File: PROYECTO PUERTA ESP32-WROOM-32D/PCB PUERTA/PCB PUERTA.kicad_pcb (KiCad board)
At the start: 2 copper layers, 91.3 x 69.2 mm, 35 parts, among them J1 LIMIT SWITCHES, J2 LLAVE, J3 Screw_Terminal_01x03, J4 Screw_Terminal_01x02, J5 ALIMENTACION, J6 MOTOR, J7 LAMP, K1 FINDER-36.11, K2 FINDER-36.11, Q1 PZT2222A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

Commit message: 20.03.2025
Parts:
- removed Q1, Q2, Q3, Q4: PZT2222A, Package_TO_SOT_SMD:SOT-223-3_TabPin2
- added C2: 100nF, Capacitor_SMD:C_0402_1005Metric, B.Cu at (110.0, 84.3)
- added C3: 100nF, Capacitor_SMD:C_0402_1005Metric, B.Cu at (110.0, 91.3)
- added C4: 100nF, Capacitor_SMD:C_0402_1005Metric, B.Cu at (110.0, 80.4)
- added C5: 100nF, Capacitor_SMD:C_0402_1005Metric, B.Cu at (110.0, 87.8)
- added C6: 100nF, Capacitor_SMD:C_0402_1005Metric, B.Cu at (109.7, 72.7)
- added C7: 22uF, Capacitor_SMD:CP_Elec_5x5.4, F.Cu at (144.2, 80.5)
- added D10: MA, LED_SMD:LED_0402_1005Metric, F.Cu at (136.2, 91.6)
- added D11: MC, LED_SMD:LED_0402_1005Metric, F.Cu at (137.7, 122.2)
- added D12: MA, LED_SMD:LED_0402_1005Metric, F.Cu at (123.3, 118.8)
- added D13: MA, LED_SMD:LED_0402_1005Metric, F.Cu at (144.4, 133.6)
- added D3: ESD9B3.3ST5G, Diode_SMD:D_SOD-923, B.Cu at (109.8, 92.8)
- added D4: ESD9B3.3ST5G, Diode_SMD:D_SOD-923, B.Cu at (109.8, 81.9)
- added D5: ESD9B3.3ST5G, Diode_SMD:D_SOD-923, B.Cu at (109.8, 89.3)
- added D6: ESD9B3.3ST5G, Diode_SMD:D_SOD-923, B.Cu at (109.7, 74.1)
- added D7: 3V3, LED_SMD:LED_0402_1005Metric, F.Cu at (120.3, 125.9)
- added D8: 5V, LED_SMD:LED_0402_1005Metric, F.Cu at (123.5, 125.9)
- added D9: 12V, LED_SMD:LED_0402_1005Metric, F.Cu at (127.3, 125.9)
- added R17: 0.1, Resistor_SMD:R_2512_6332Metric, F.Cu at (135.2, 95.8)
- added R18: 220, Resistor_SMD:R_0402_1005Metric, F.Cu at (135.8, 122.2)
- added R19: 220, Resistor_SMD:R_0402_1005Metric, F.Cu at (121.4, 118.8)
- added R20: 220, Resistor_SMD:R_0402_1005Metric, F.Cu at (142.5, 133.6)
- added U2: MMUN2233LT1G, LIBRERIA PERSONAL:SOT-23-3_1P4X3P040_ONS-L, F.Cu at (135.3, 87.9)
- added U3: LM358, LIBRERIA PERSONAL:lm358, F.Cu at (135.3, 103.7)
- added U4: MMUN2233LT1G, LIBRERIA PERSONAL:SOT-23-3_1P4X3P040_ONS-L, F.Cu at (122.4, 115.4)
- added U5: MMUN2233LT1G, LIBRERIA PERSONAL:SOT-23-3_1P4X3P040_ONS-L, F.Cu at (143.5, 129.6)
- added U6: MMUN2233LT1G, LIBRERIA PERSONAL:SOT-23-3_1P4X3P040_ONS-L, F.Cu at (136.7, 118.6)
- BZ1: footprint Buzzer_Beeper:Buzzer_CUI_CPT-9019S-SMT -> Buzzer_Beeper:Buzzer_TDK_PS1240P02BT_D12.2mm_H6.5mm
- C1: value 22u -> 100nF; moved to B.Cu
- D1: value MA -> ESD9B3.3ST5G; footprint LED_SMD:LED_0402_1005Metric -> Diode_SMD:D_SOD-923; moved to B.Cu
- D2: value MC -> ESD9B3.3ST5G; footprint LED_SMD:LED_0402_1005Metric -> Diode_SMD:D_SOD-923; moved to B.Cu
- J5: value ALIMENTACION -> Screw_Terminal_01x04; footprint TerminalBlock:TerminalBlock_bornier-2_P5.08mm -> TerminalBlock:TerminalBlock_bornier-4_P5.08mm
- R10, R12, R13, R14: moved to B.Cu
- R15: value 220 -> 100k; footprint Resistor_SMD:R_0402_1005Metric -> Capacitor_SMD:C_0402_1005Metric
- R16: value 1k -> 20k; footprint Resistor_SMD:R_0402_1005Metric -> Capacitor_SMD:C_0402_1005Metric
- R7, R8, R9: value 1k -> 220
- SW1: footprint Button_Switch_SMD:SW_DIP_SPSTx04_Slide_9.78x12.34mm_W8.61mm_P2.54mm -> Button_Switch_SMD:SW_DIP_SPSTx04_Slide_KingTek_DSHP04TS_W7.62mm_P1.27mm
- moved C1 80.9 mm to (109.9, 75.8), turned to 0 degrees
- moved BZ1 61.4 mm to (109.1, 119.5), turned to 90 degrees
- moved K1 51.7 mm to (143.8, 103.1), turned to 90 degrees
- moved K2 50.5 mm to (143.9, 122.3), turned to 90 degrees
- moved J6 50.0 mm to (151.6, 80.3), turned to 0 degrees
- moved R14 49.9 mm to (123.2, 79.1)
- moved R7 45.5 mm to (118.7, 126.0), turned to -90 degrees
- moved D2 44.5 mm to (109.8, 85.7)
- moved D1 44.0 mm to (109.9, 77.2)
- moved R13 43.5 mm to (123.2, 76.6)
- moved R8 41.8 mm to (122.1, 125.9), turned to -90 degrees
- moved R9 38.3 mm to (125.5, 125.9), turned to -90 degrees
- moved J5 33.9 mm to (134.0, 131.6), turned to 180 degrees
- moved R12 31.7 mm to (123.2, 74.1)
- moved R6 31.4 mm to (107.6, 74.1)
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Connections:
- C1 pad 1: +5V -> LSA
- D1 pad 2: Net-(D1-A) -> LSA
- D2 pad 2: Net-(D2-A) -> KEYA
- J5 pad 2: +5V -> +12V
- K1 pad 12: +5V -> +12V
- K1 pad 14: GND -> RefCorriente
- K1 pad A1: +5V -> +12V
- K2 pad 12: +5V -> +12V
- K2 pad 14: GND -> RefCorriente
- K2 pad A1: +5V -> +12V
- R10 pad 2: Net-(U1-D27) -> Net-(U1-D13)
- R11 pad 1: Net-(D1-A) -> Net-(D10-A)
- R12 pad 1: MA -> +3.3V
- R12 pad 2: Net-(Q1-B) -> Net-(U1-D12)
- R13 pad 1: LAMP -> +3.3V
- R13 pad 2: Net-(Q2-B) -> Net-(U1-D14)
- R14 pad 1: BUZZER -> +3.3V
- R14 pad 2: Net-(Q3-B) -> Net-(U1-D27)
- R15 pad 1: Net-(D2-A) -> Net-(U1-D33)
- R15 pad 2: MC -> Net-(U3A--)
- R16 pad 1: MC -> Net-(U3A--)
- R16 pad 2: Net-(Q4-B) -> GND
- R3 pad 2: FTC -> PP
- R4 pad 2: PP -> FTC
- R5 pad 2: LSC -> KEYC
- R6 pad 2: KEYC -> LSC
- R7 pad 1: +3.3V -> Net-(D7-A)
- R7 pad 2: Net-(U1-D13) -> +3.3V
- R8 pad 1: +3.3V -> Net-(D8-A)
- R8 pad 2: Net-(U1-D12) -> +5V
- R9 pad 1: +3.3V -> Net-(D9-A)
- R9 pad 2: Net-(U1-D14) -> +12V
- U1 pad 1: +3.3V -> unconnected-(U1-3V3-Pad1)
- U1 pad 22: unconnected-(U1-D33-Pad22) -> Net-(U1-D33)
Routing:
- net +12V: track 0.00 -> 76.7 mm
- net +3.3V: track 51.1 -> 123.8 mm, vias 0 -> 2
- net RefCorriente: track 0.00 -> 55.5 mm, vias 0 -> 1
- net +5V: track 222.4 -> 183.9 mm
- net MO1: track 58.0 -> 23.7 mm
- net MC: track 10.4 -> 43.7 mm, vias 0 -> 2
- net FTC: track 30.8 -> 61.2 mm
- net KEYC: track 14.7 -> 42.2 mm
- net Net-(U2-COLLECTOR): track 36.8 -> 10.2 mm, vias 1 -> 0
- net Net-(U6-COLLECTOR): track 38.0 -> 11.4 mm, vias 1 -> 0
- net Net-(U1-D33): track 0.00 -> 21.8 mm, vias 0 -> 1
- net PP: track 30.9 -> 52.3 mm
- net MO2: track 20.9 -> 42.1 mm
- net Net-(J7-Pin_2): track 30.2 -> 9.75 mm, vias 1 -> 0
- net KEYA: track 19.7 -> 36.9 mm
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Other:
- board size 91.3 x 69.2 mm -> 77 x 79.6 mm

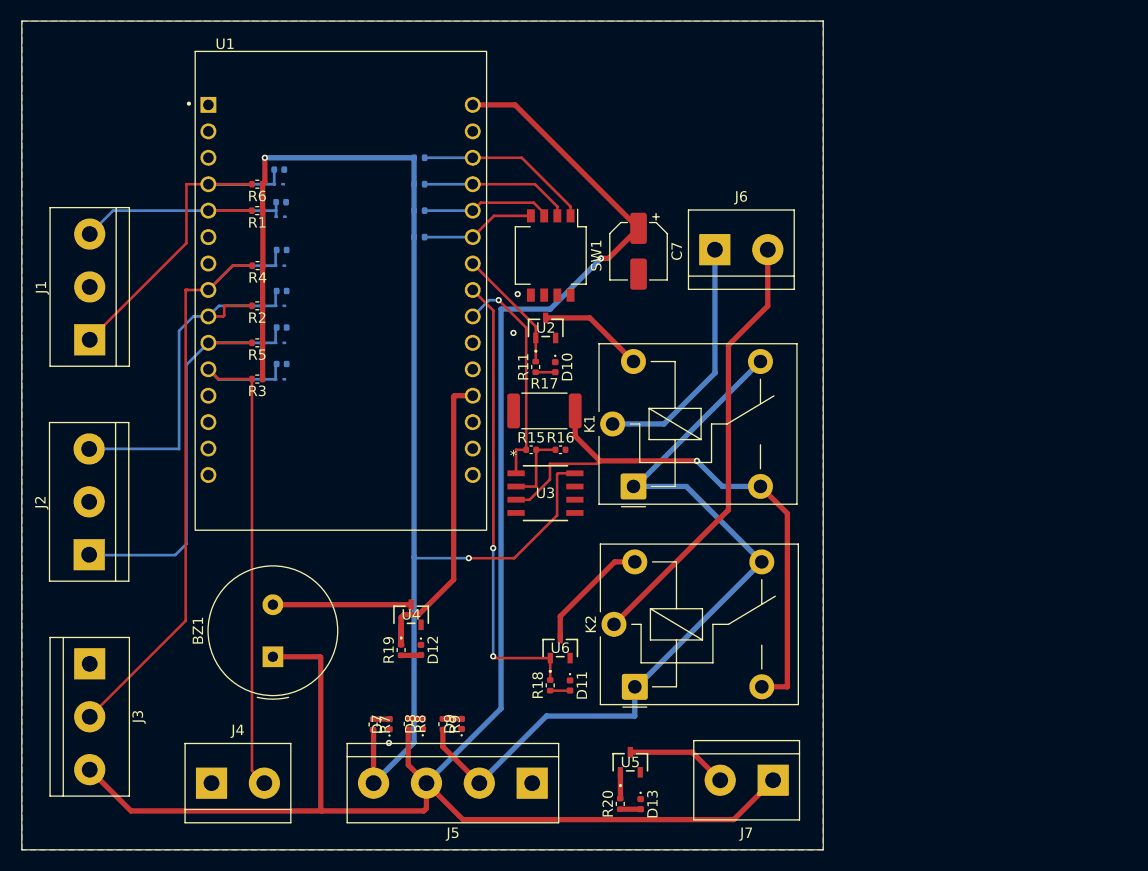
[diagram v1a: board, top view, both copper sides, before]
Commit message: agregando emulador NE555
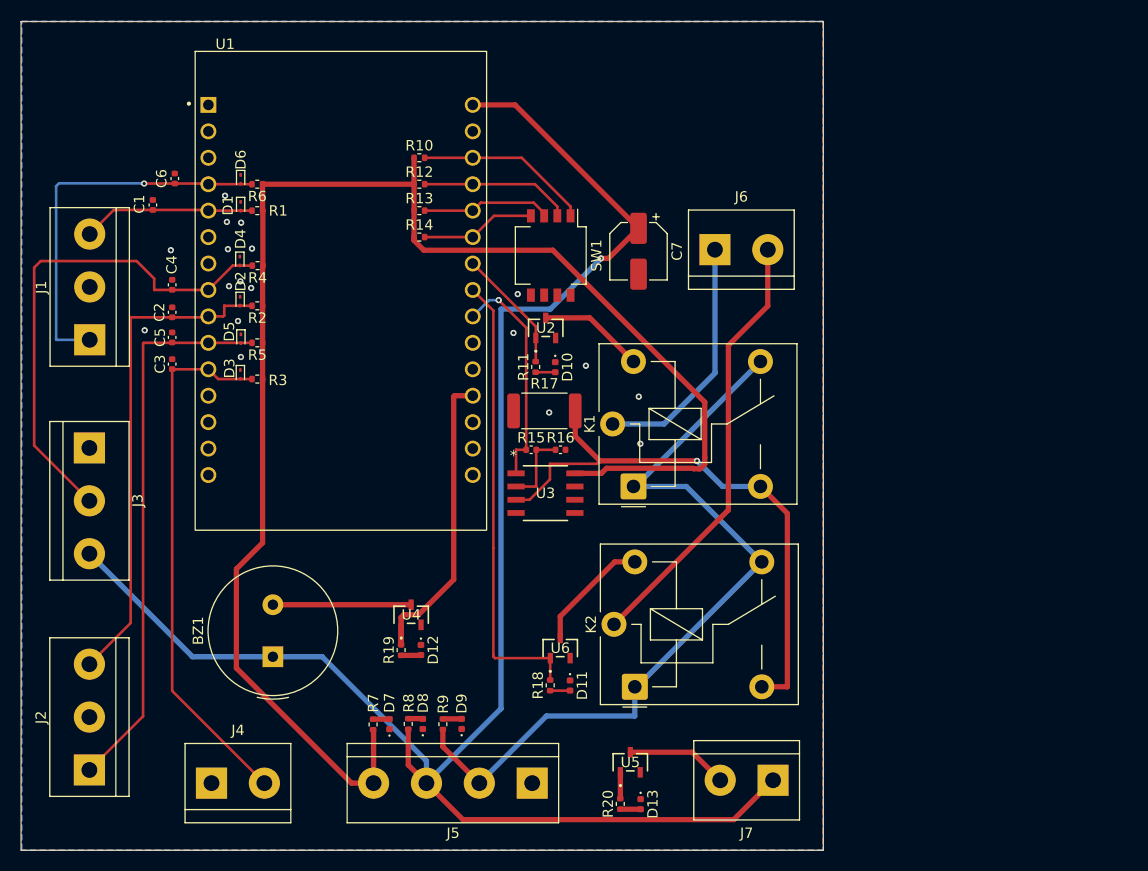
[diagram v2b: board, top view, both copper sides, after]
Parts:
- C1, C2, C3, C4, C5, C6, D1, D2, D3, D4, D5, D6, R10, R12, R13, R14: moved to F.Cu
- moved J3 20.7 mm to (91.5, 99.4)
- moved J2 20.7 mm to (91.5, 130.3)
- moved C1 12.3 mm to (97.6, 76.0), turned to 90 degrees
- moved C4 11.0 mm to (99.4, 83.7), turned to 90 degrees
- moved C2 10.7 mm to (99.4, 86.4), turned to 90 degrees
- moved C5 10.6 mm to (99.4, 88.8), turned to 90 degrees
- moved C3 10.5 mm to (99.4, 91.3), turned to 90 degrees
- moved C6 10.1 mm to (99.7, 73.5), turned to 90 degrees
- moved D1 3.97 mm to (106.0, 76.2), turned to -90 degrees
- moved D4 3.88 mm to (105.9, 81.4), turned to -90 degrees
- moved D2 3.85 mm to (106.0, 85.3), turned to -90 degrees
- moved D3 3.83 mm to (106.0, 92.3), turned to -90 degrees
- moved D5 3.77 mm to (106.0, 88.9), turned to -90 degrees
- moved D6 3.68 mm to (106.0, 73.6), turned to -90 degrees
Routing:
- net +3.3V: track 123.8 -> 146.2 mm, vias 2 -> 0
- net +5V: track 183.9 -> 170.7 mm
- net FTC: track 61.2 -> 48.6 mm
- net KEYC: track 42.2 -> 53.6 mm
- net KEYA: track 36.9 -> 47.7 mm
- net LSA: track 24.4 -> 16.6 mm
- net LSC: track 32.9 -> 37.0 mm, vias 0 -> 1
- net PP: track 52.3 -> 51.5 mm
- net MC: track 43.7 -> 43.8 mm, vias 2 -> 0
- net GND: vias 3 -> 18
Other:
- board size 77 x 79.6 mm -> 77.1 x 79.6 mm
